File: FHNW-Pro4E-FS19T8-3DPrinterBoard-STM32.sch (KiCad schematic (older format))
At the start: 33 parts, among them J101 Screw_Terminal_01x02, T101 BUK963R3-60E, U101 LM2675M-3.3, U102 LM2675M-5

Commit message: user LED + fixes in Layout
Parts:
- added G101: SYM_Serial_No, FHNW-Pro4E-FS19T8-Library:Label_Serial_Number_6x20, symbol FHNW-Pro4E-FS19T8-Library:SYM_Serial_No
- added G102: SYM_FHNW_Logo, FHNW-Pro4E-FS19T8-Library:Logo_FHNW_03x05mm, symbol FHNW-Pro4E-FS19T8-Library:SYM_FHNW_Logo
- added LOGO101: OSHW-LOGOM-COPPER, Symbols:OSHW-Logo2_9.8x8mm_SilkScreen, symbol SparkFun-Aesthetics:OSHW-LOGOM-COPPER
- D105: value D_Zener -> BZT52H-B7V5; footprint Diodes_SMD:D_SMB -> Diodes_SMD:D_SOD-123
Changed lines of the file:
@@
 AR Path="/5CA39F21/5CC929A8" Ref="T?"  Part="1"
 AR Path="/5CC929A8" Ref="T101"  Part="1"
-F 0 "T101" V 2000 7450 50  0000 L CNN
+F 0 "T101" V 2000 6950 50  0000 L CNN
 F 1 "BUK963R3-60E" V 2100 6950 50  0000 L CNN
 F 2 "Package_TO_SOT_SMD:TO-263-2" H 2700 6850 50  0001 C CNN
@@
 P 2250 7100
 F 0 "D105" V 2204 7179 50  0000 L CNN
-F 1 "D_Zener" V 2295 7179 50  0000 L CNN
-F 2 "Diodes_SMD:D_SMB" H 2250 7100 50  0001 C CNN
+F 1 "BZT52H-B7V5" V 2295 7179 50  0000 L CNN
+F 2 "Diodes_SMD:D_SOD-123" H 2250 7100 50  0001 C CNN
 F 3 "~" H 2250 7100 50  0001 C CNN
 	1    2250 7100
@@
 U 1 1 5CC0EDCA
 P 1350 6850
-F 0 "D106" V 1304 6640 50  0000 R CNN
-F 1 "APHBM2012LSURKZGKC" V 1395 6640 50  0000 R CNN
+F 0 "D106" V 1650 7200 50  0000 R CNN
+F 1 "APHBM2012LSURKZGKC" V 1850 7700 50  0000 R CNN
 F 2 "FHNW-Pro4E-FS19T8-Library:LED_Kingbright_SMD4_2.0x1.25" H 1380 6850 50  0001 C CNN
 F 3 "~" H 1380 6850 50  0001 C CNN
@@
 	1    0    0    -1
 $EndComp
+$Comp
+L FHNW-Pro4E-FS19T8-Library:SYM_FHNW_Logo G102
+U 1 1 5CC56D8C
+P 950 1750
+F 0 "G102" H 1178 1696 50  0000 L CNN
+F 1 "SYM_FHNW_Logo" H 1178 1605 50  0000 L CNN
+F 2 "FHNW-Pro4E-FS19T8-Library:Logo_FHNW_03x05mm" H 950 1750 50  0001 C CNN
+F 3 "" H 950 1750 50  0001 C CNN
+	1    950  1750
+	1    0    0    -1
+$EndComp
+$Comp
+L FHNW-Pro4E-FS19T8-Library:SYM_Serial_No G101
+U 1 1 5CC57A3F
+P 1050 1350
+F 0 "G101" H 1378 1246 50  0000 L CNN
+F 1 "SYM_Serial_No" H 1378 1155 50  0000 L CNN
+F 2 "FHNW-Pro4E-FS19T8-Library:Label_Serial_Number_6x20" H 1050 1350 50  0001 C CNN
+F 3 "" H 1050 1350 50  0001 C CNN
+	1    1050 1350
+	1    0    0    -1
+$EndComp
+$Comp
+L SparkFun-Aesthetics:OSHW-LOGOM-COPPER LOGO101
+U 1 1 5CC5A1CC
+P 1200 2300
+F 0 "LOGO101" H 1200 2550 45  0001 C CNN
+F 1 "OSHW-LOGOM-COPPER" H 1200 1900 45  0001 C CNN
+F 2 "Symbols:OSHW-Logo2_9.8x8mm_SilkScreen" H 1200 2600 20  0001 C CNN
+F 3 "" H 1200 2300 50  0001 C CNN
+F 4 "XXX-00000" H 1678 2235 60  0001 L CNN "Field4"
+	1    1200 2300
+	1    0    0    -1
+$EndComp

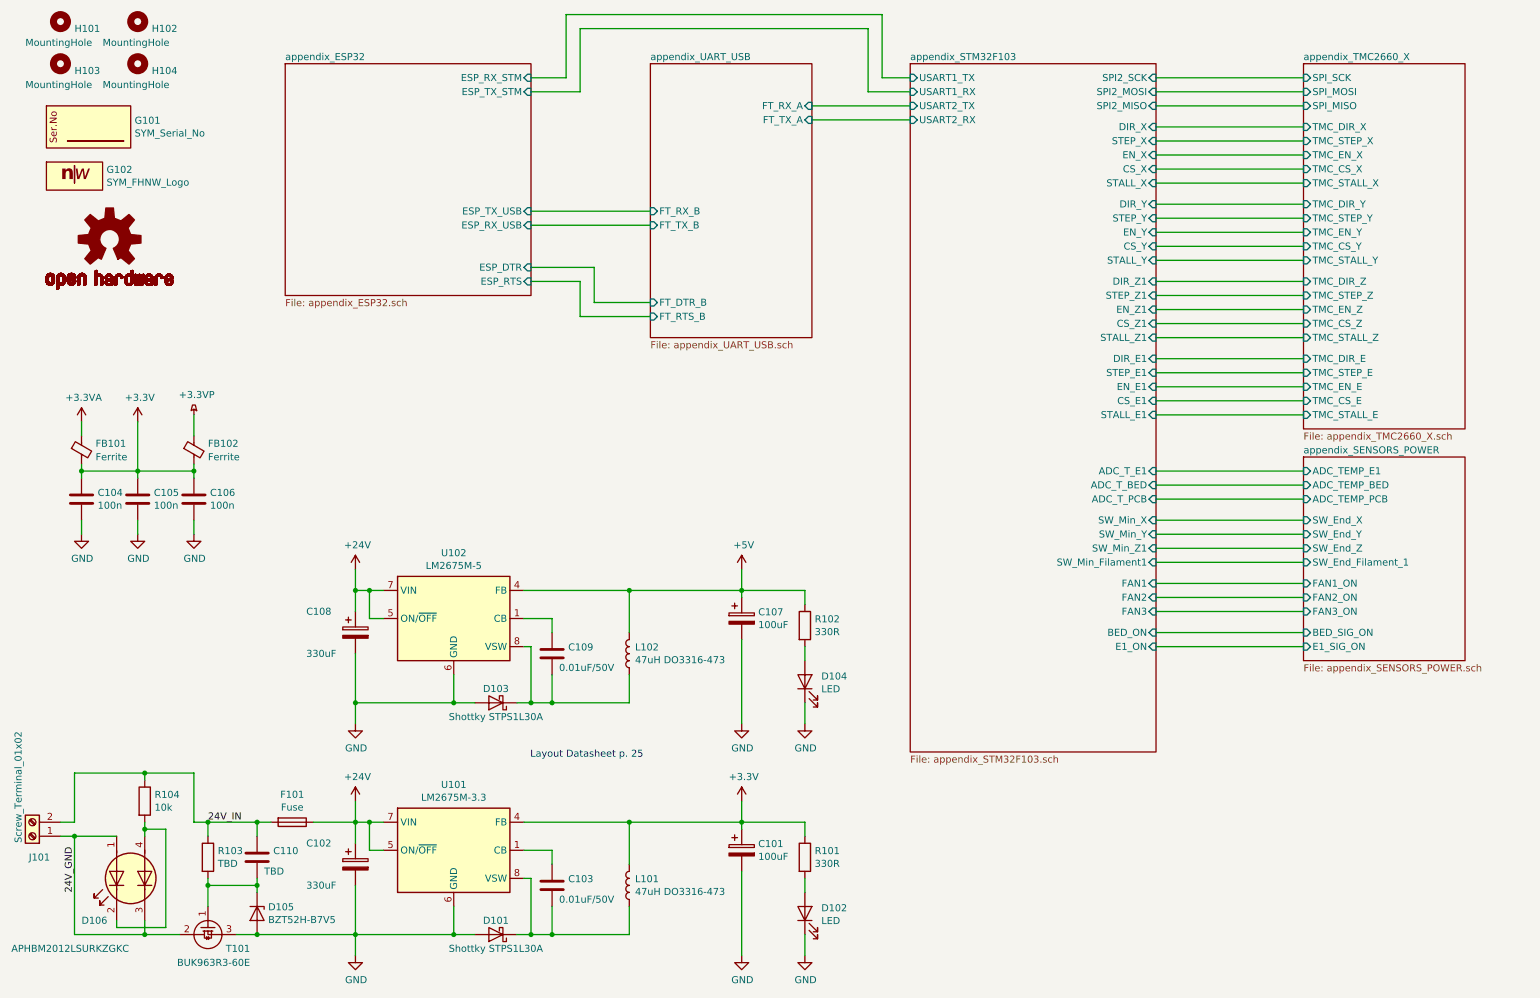
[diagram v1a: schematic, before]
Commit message: TVS protection, BOOT1 pin, user BTN
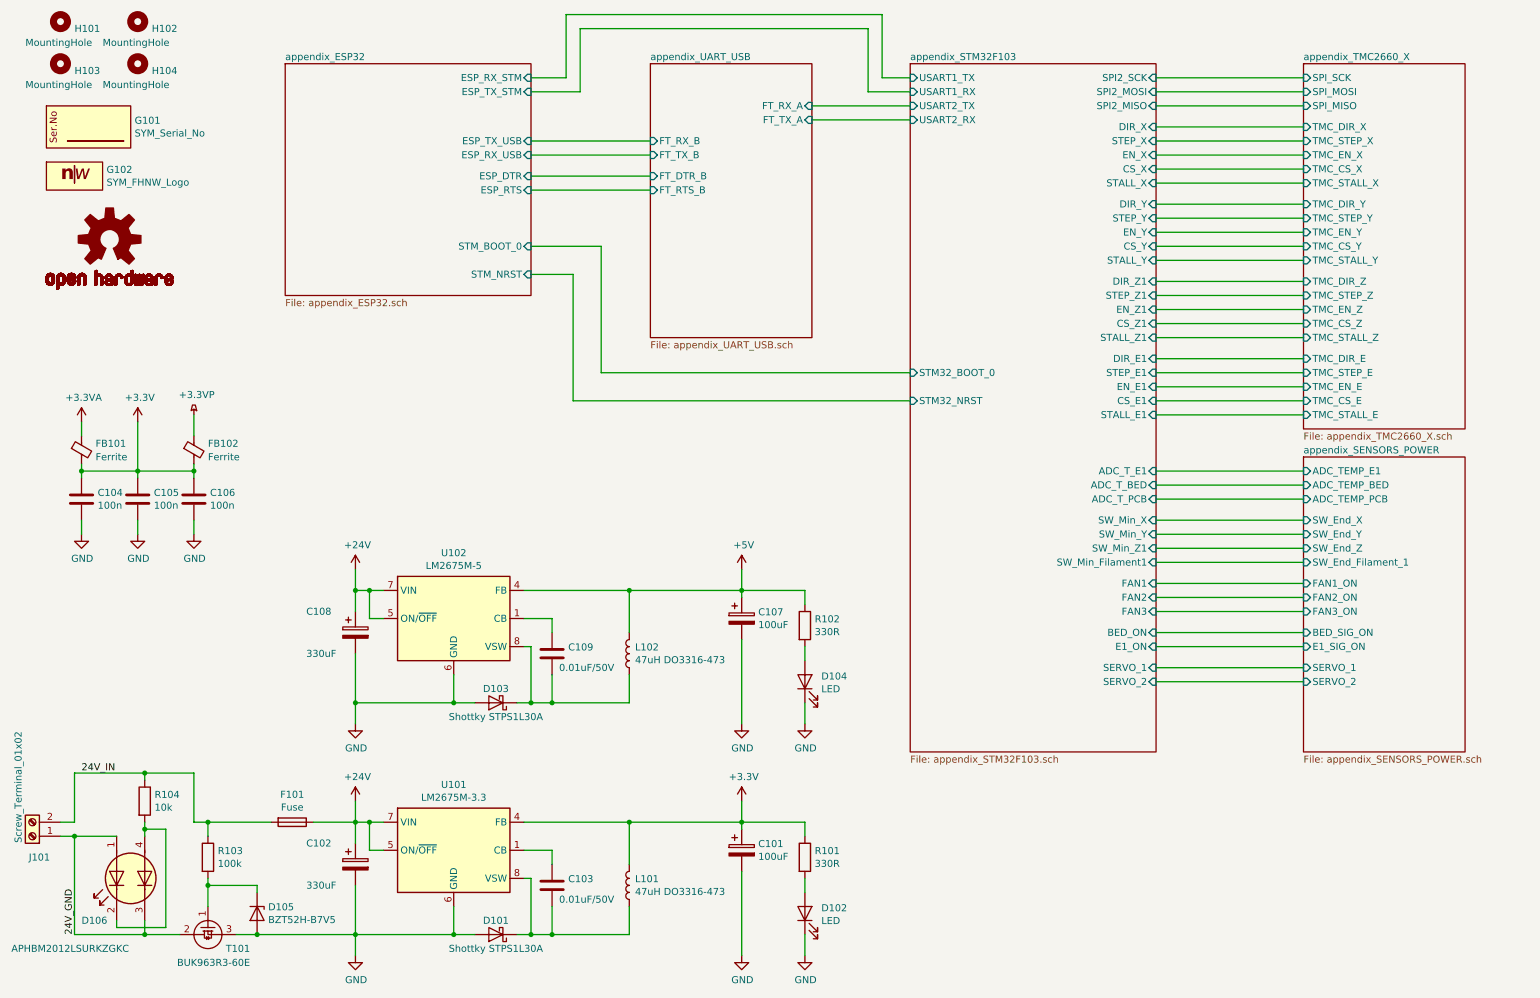
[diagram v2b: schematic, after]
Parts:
- removed C110: TBD, Capacitors_SMD:C_0603, symbol Device:C
- R103: value TBD -> 100k
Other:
- note removed: "Layout Datasheet p. 25"
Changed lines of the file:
@@
 F39 "SW_Min_Z1" I R 8650 4500 50
 F40 "SW_Min_Filament1" I R 8650 4600 50
+F41 "STM32_BOOT_0" I L 6900 3250 50
+F42 "STM32_NRST" I L 6900 3450 50
+F43 "SERVO_1" I R 8650 5350 50
+F44 "SERVO_2" I R 8650 5450 50
 $EndSheet
 $Sheet
@@
 F2 "ESP_TX_STM" I R 4200 1250 50
 F3 "ESP_RX_STM" I R 4200 1150 50
-F4 "ESP_DTR" I R 4200 2500 50
-F5 "ESP_RTS" I R 4200 2600 50
-F6 "ESP_RX_USB" I R 4200 2200 50
-F7 "ESP_TX_USB" I R 4200 2100 50
+F4 "ESP_DTR" I R 4200 1850 50
+F5 "ESP_RTS" I R 4200 1950 50
+F6 "ESP_RX_USB" I R 4200 1700 50
+F7 "ESP_TX_USB" I R 4200 1600 50
+F8 "STM_BOOT_0" I R 4200 2350 50
+F9 "STM_NRST" I R 4200 2550 50
 $EndSheet
 $Sheet
@@
 Wire Wire Line
 	3050 6450 2950 6450
-Text Notes 5000 6000 2    50   ~ 0
-Layout Datasheet p. 25
 $Comp
 L power:+5V #PWR01
@@
 Wire Wire Line
 	6150 5600 6150 5750
-Wire Wire Line
-	5050 2750 4650 2750
-Wire Wire Line
-	4650 2750 4650 2500
-Wire Wire Line
-	4650 2500 4200 2500
 $Sheet
 S 5050 1050 1150 1950
@@
 F0 "appendix_UART_USB" 50
 F1 "appendix_UART_USB.sch" 50
-F2 "FT_RX_B" I L 5050 2100 50
-F3 "FT_TX_B" I L 5050 2200 50
+F2 "FT_RX_B" I L 5050 1600 50
+F3 "FT_TX_B" I L 5050 1700 50
 F4 "FT_RX_A" I R 6200 1350 50
 F5 "FT_TX_A" I R 6200 1450 50
-F6 "FT_DTR_B" I L 5050 2750 50
-F7 "FT_RTS_B" I L 5050 2850 50
+F6 "FT_DTR_B" I L 5050 1850 50
+F7 "FT_RTS_B" I L 5050 1950 50
 $EndSheet
 Wire Wire Line
-	5050 2100 4200 2100
+	5050 1600 4200 1600
 Wire Wire Line
-	4200 2200 5050 2200
+	4200 1700 5050 1700
 Wire Wire Line
 	4200 1150 4450 1150
@@
 Wire Wire Line
 	9700 4950 8650 4950
-Wire Wire Line
-	4200 2600 4550 2600
-Wire Wire Line
-	4550 2600 4550 2850
-Wire Wire Line
-	4550 2850 5050 2850
 $Comp
 L Mechanical:MountingHole H101
@@
 P 1900 6700
 F 0 "R103" H 1970 6746 50  0000 L CNN
-F 1 "TBD" H 1970 6655 50  0000 L CNN
+F 1 "100k" H 1970 6655 50  0000 L CNN
 F 2 "Resistors_SMD:R_0603" V 1830 6700 50  0001 C CNN
 F 3 "~" H 1900 6700 50  0001 C CNN
@@
 	1    0    0    -1
 $EndComp
-$Comp
-L Device:C C110
-U 1 1 5CCAF09E
-P 2250 6700
-F 0 "C110" H 2365 6746 50  0000 L CNN
-F 1 "TBD" H 2300 6600 50  0000 L CNN
-F 2 "Capacitors_SMD:C_0603" H 2288 6550 50  0001 C CNN
-F 3 "~" H 2250 6700 50  0001 C CNN
-	1    2250 6700
-	1    0    0    -1
-$EndComp
 Wire Wire Line
 	2100 7250 2250 7250
@@
 	1900 7050 1900 6900
 Wire Wire Line
-	2250 6850 2250 6900
-Wire Wire Line
 	2250 6900 1900 6900
 Connection ~ 1900 6900
@@
 	1900 6900 1900 6850
 Wire Wire Line
-	2250 6550 2250 6450
-Connection ~ 2250 6450
-Wire Wire Line
-	2250 6450 2350 6450
-Wire Wire Line
 	1900 6450 1900 6550
-Wire Wire Line
-	1900 6450 2250 6450
 $Comp
 L Device:D_Zener D105
@@
 Wire Wire Line
 	2250 6950 2250 6900
-Connection ~ 2250 6900
 $Comp
 L Device:Fuse F?
@@
 $EndComp
 $Sheet
-S 9700 3850 1150 1450
+S 9700 3850 1150 2100
 U 5CA39F21
 F0 "appendix_SENSORS_POWER" 50
@@
 F12 "E1_SIG_ON" I L 9700 5200 50
 F13 "SW_End_Filament_1" I L 9700 4600 50
+F14 "SERVO_1" I L 9700 5350 50
+F15 "SERVO_2" I L 9700 5450 50
 $EndSheet
 Wire Wire Line
@@
 Wire Wire Line
 	9700 5200 8650 5200
-Text Label 950  6950 1    50   ~ 0
+Text Label 950  7250 1    50   ~ 0
 24V_GND
-Text Label 1900 6450 0    50   ~ 0
+Text Label 1000 6100 0    50   ~ 0
 24V_IN
 $Comp
@@
 	1    0    0    -1
 $EndComp
+Wire Wire Line
+	1900 6450 2350 6450
+Wire Wire Line
+	9700 5350 8650 5350
+Wire Wire Line
+	9700 5450 8650 5450
+Wire Wire Line
+	5050 1850 4200 1850
+Wire Wire Line
+	4200 1950 5050 1950
+Wire Wire Line
+	6900 3250 4700 3250
+Wire Wire Line
+	4700 3250 4700 2350
+Wire Wire Line
+	4700 2350 4200 2350
+Wire Wire Line
+	6900 3450 4500 3450
+Wire Wire Line
+	4500 3450 4500 2550
+Wire Wire Line
+	4500 2550 4200 2550
 $EndSCHEMATC

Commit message: finished up for final review
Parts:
- removed C105: 100n, Capacitors_SMD:C_0603, symbol Device:C
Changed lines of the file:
@@
-$EndComp
-$Comp
-L power:GND #PWR0126
-U 1 1 5CC014A2
-P 1400 4400
-F 0 "#PWR0126" H 1400 4150 50  0001 C CNN
-F 1 "GND" H 1405 4227 50  0000 C CNN
-F 2 "" H 1400 4400 50  0001 C CNN
-F 3 "" H 1400 4400 50  0001 C CNN
-	1    1400 4400
-	1    0    0    -1
 $EndComp
 $Comp
@@
 Wire Wire Line
 	1000 4400 1000 4300
-Wire Wire Line
-	1400 4400 1400 4300
-Wire Wire Line
-	1400 4000 1400 3950
 Wire Wire Line
 	1400 3950 1000 3950
@@
 	1450 6100 1800 6100
 $Comp
-L Device:C C105
-U 1 1 5CC01495
-P 1400 4150
-F 0 "C105" H 1515 4196 50  0000 L CNN
-F 1 "100n" H 1515 4105 50  0000 L CNN
-F 2 "Capacitors_SMD:C_0603" H 1438 4000 50  0001 C CNN
-F 3 "~" H 1400 4150 50  0001 C CNN
-	1    1400 4150
-	1    0    0    -1
-$EndComp
-$Comp
 L FHNW-Pro4E-FS19T8-Library:SYM_FHNW_Logo G102
 U 1 1 5CC56D8C
@@
 Wire Wire Line
 	4500 2550 4200 2550
+$Comp
+L power:PWR_FLAG #FLG0101
+U 1 1 5E688628
+P 700 5000
+F 0 "#FLG0101" H 700 5075 50  0001 C CNN
+F 1 "PWR_FLAG" V 700 5350 50  0000 C CNN
+F 2 "" H 700 5000 50  0001 C CNN
+F 3 "~" H 700 5000 50  0001 C CNN
+	1    700  5000
+	-1   0    0    1
+$EndComp
+$Comp
+L power:+3.3VA #PWR0126
+U 1 1 5E68AEEF
+P 700 5000
+F 0 "#PWR0126" H 700 4850 50  0001 C CNN
+F 1 "+3.3VA" H 715 5173 50  0000 C CNN
+F 2 "" H 700 5000 50  0001 C CNN
+F 3 "" H 700 5000 50  0001 C CNN
+	1    700  5000
+	1    0    0    -1
+$EndComp
+$Comp
+L power:PWR_FLAG #FLG0102
+U 1 1 5E693379
+P 1000 5000
+F 0 "#FLG0102" H 1000 5075 50  0001 C CNN
+F 1 "PWR_FLAG" V 1000 5350 50  0000 C CNN
+F 2 "" H 1000 5000 50  0001 C CNN
+F 3 "~" H 1000 5000 50  0001 C CNN
+	1    1000 5000
+	-1   0    0    1
+$EndComp
+$Comp
+L power:+3.3V #PWR0237
+U 1 1 5E69357A
+P 1000 5000
+F 0 "#PWR0237" H 1000 4850 50  0001 C CNN
+F 1 "+3.3V" H 1015 5173 50  0000 C CNN
+F 2 "" H 1000 5000 50  0001 C CNN
+F 3 "" H 1000 5000 50  0001 C CNN
+	1    1000 5000
+	1    0    0    -1
+$EndComp
+$Comp
+L power:+3.3VP #PWR0246
+U 1 1 5E69A805
+P 1300 5000
+F 0 "#PWR0246" H 1450 4950 50  0001 C CNN
+F 1 "+3.3VP" H 1320 5143 50  0000 C CNN
+F 2 "" H 1300 5000 50  0001 C CNN
+F 3 "" H 1300 5000 50  0001 C CNN
+	1    1300 5000
+	1    0    0    -1
+$EndComp
+$Comp
+L power:PWR_FLAG #FLG0103
+U 1 1 5E69AB83
+P 1300 5000
+F 0 "#FLG0103" H 1300 5075 50  0001 C CNN
+F 1 "PWR_FLAG" V 1300 5350 50  0000 C CNN
+F 2 "" H 1300 5000 50  0001 C CNN
+F 3 "~" H 1300 5000 50  0001 C CNN
+	1    1300 5000
+	-1   0    0    1
+$EndComp
+$Comp
+L power:+24V #PWR?
+U 1 1 5E69ACDE
+P 1600 5000
+AR Path="/5CA3FF44/5E69ACDE" Ref="#PWR?"  Part="1"
+AR Path="/5E69ACDE" Ref="#PWR0251"  Part="1"
+F 0 "#PWR0251" H 1600 4850 50  0001 C CNN
+F 1 "+24V" H 1615 5173 50  0000 C CNN
+F 2 "" H 1600 5000 50  0001 C CNN
+F 3 "" H 1600 5000 50  0001 C CNN
+	1    1600 5000
+	1    0    0    -1
+$EndComp
+$Comp
+L power:PWR_FLAG #FLG0104
+U 1 1 5E69B096
+P 1600 5000
+F 0 "#FLG0104" H 1600 5075 50  0001 C CNN
+F 1 "PWR_FLAG" V 1600 5350 50  0000 C CNN
+F 2 "" H 1600 5000 50  0001 C CNN
+F 3 "~" H 1600 5000 50  0001 C CNN
+	1    1600 5000
+	-1   0    0    1
+$EndComp
+$Comp
+L power:PWR_FLAG #FLG0105
+U 1 1 5E6A206A
+P 1900 5000
+F 0 "#FLG0105" H 1900 5075 50  0001 C CNN
+F 1 "PWR_FLAG" V 1900 5350 50  0000 C CNN
+F 2 "" H 1900 5000 50  0001 C CNN
+F 3 "~" H 1900 5000 50  0001 C CNN
+	1    1900 5000
+	-1   0    0    1
+$EndComp
+$Comp
+L power:+5V #PWR0265
+U 1 1 5E6A2352
+P 1900 5000
+F 0 "#PWR0265" H 1900 4850 50  0001 C CNN
+F 1 "+5V" H 1915 5173 50  0000 C CNN
+F 2 "" H 1900 5000 50  0001 C CNN
+F 3 "" H 1900 5000 50  0001 C CNN
+	1    1900 5000
+	1    0    0    -1
+$EndComp
+$Comp
+L power:VBUS #PWR?
+U 1 1 5E6AB26A
+P 2200 5000
+AR Path="/5CA3CC17/5E6AB26A" Ref="#PWR?"  Part="1"
+AR Path="/5E6AB26A" Ref="#PWR?"  Part="1"
+F 0 "#PWR?" H 2200 4850 50  0001 C CNN
+F 1 "VBUS" H 2215 5173 50  0000 C CNN
+F 2 "" H 2200 5000 50  0001 C CNN
+F 3 "" H 2200 5000 50  0001 C CNN
+	1    2200 5000
+	1    0    0    -1
+$EndComp
+$Comp
+L power:PWR_FLAG #FLG?
+U 1 1 5E6BE425
+P 2200 5000
+F 0 "#FLG?" H 2200 5075 50  0001 C CNN
+F 1 "PWR_FLAG" V 2200 5350 50  0000 C CNN
+F 2 "" H 2200 5000 50  0001 C CNN
+F 3 "~" H 2200 5000 50  0001 C CNN
+	1    2200 5000
+	-1   0    0    1
+$EndComp
 $EndSCHEMATC

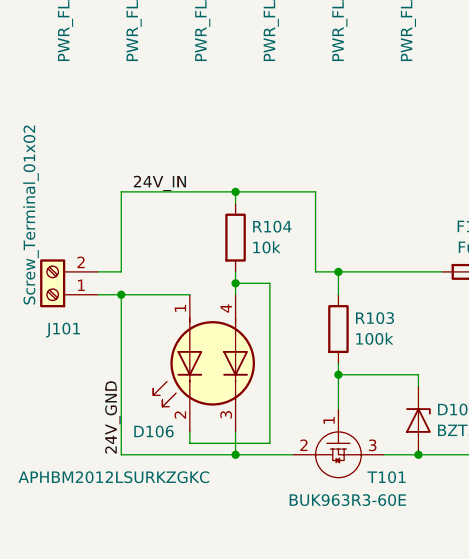
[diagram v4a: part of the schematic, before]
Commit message: changed Layout to use all Interrupt Pins
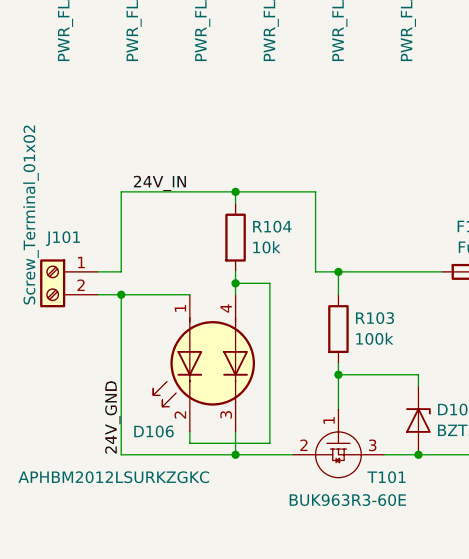
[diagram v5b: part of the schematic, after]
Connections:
- net 24V_GND: now also J101.2 (Pin_2); no longer J101.1 (Pin_1)
- net 24V_IN: now also J101.1 (Pin_1); no longer J101.2 (Pin_2)
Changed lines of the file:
@@
 L Connector:Screw_Terminal_01x02 J101
 U 1 1 5CD68AD6
-P 650 6550
-F 0 "J101" H 600 6700 50  0000 C CNN
-F 1 "Screw_Terminal_01x02" V 750 6200 50  0000 C CNN
-F 2 "Connectors_Terminal_Blocks:TerminalBlock_Altech_AK300-2_P5.00mm" H 650 6550 50  0001 C CNN
-F 3 "~" H 650 6550 50  0001 C CNN
-	1    650  6550
-	-1   0    0    1
+P 650 6450
+F 0 "J101" H 600 6600 50  0000 C CNN
+F 1 "Screw_Terminal_01x02" V 750 6700 50  0000 C CNN
+F 2 "Connectors_Terminal_Blocks:TerminalBlock_Altech_AK300-2_P5.00mm" H 650 6450 50  0001 C CNN
+F 3 "~" H 650 6450 50  0001 C CNN
+	1    650  6450
+	-1   0    0    -1
 $EndComp
 Wire Wire Line
